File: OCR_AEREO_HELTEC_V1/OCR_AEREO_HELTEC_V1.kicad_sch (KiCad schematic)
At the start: 28 parts, among them J1 INCLINOMETRO, J10 Conn_01x02_Pin, J11 Conn_01x02_Pin, J13 Conn_01x04_Socket, J14 MODULO SD, J15 Conn_01x03_Pin, J16 Conn_01x04_Socket, J17 Screw_Terminal_01x03, J18 Screw_Terminal_01x03, J19 Screw_Terminal_01x02, J3 Conn_01x18_Pin, J4 Conn_01x02_Pin, J5 Conn_01x02_Pin, J6 Screw_Terminal_01x04, J7 Screw_Terminal_01x02, J8 Conn_01x02_Pin, J9 Conn_01x02_Pin, U2 MAX3232

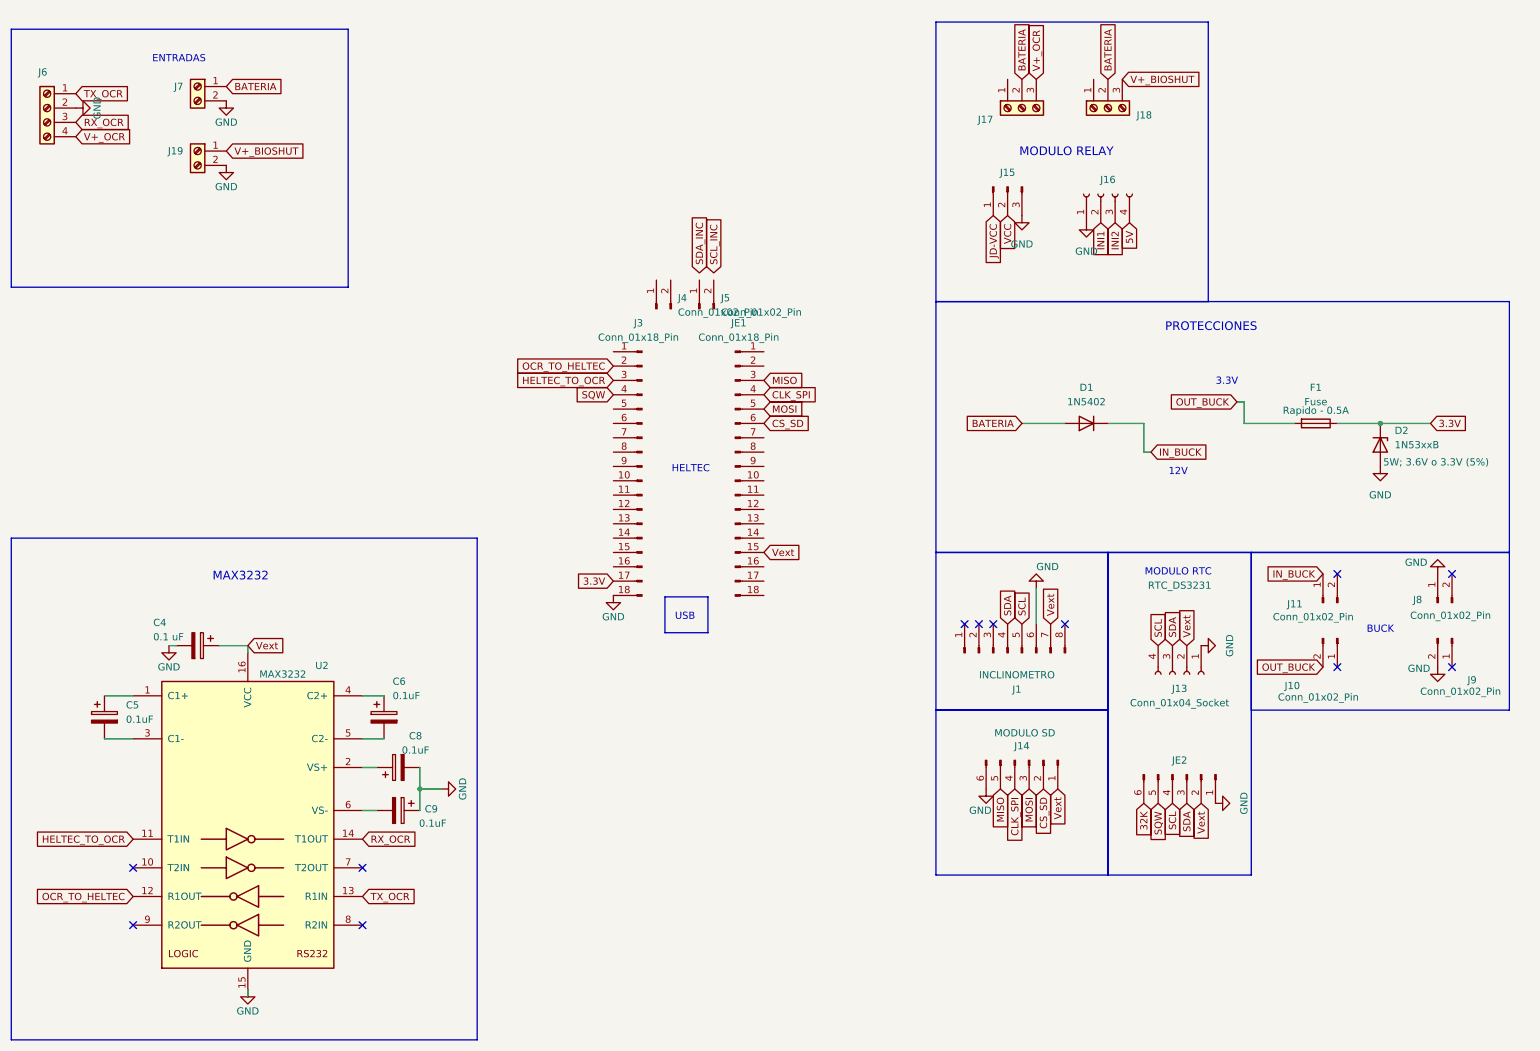
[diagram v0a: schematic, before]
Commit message: Actualizacion de placa
Incluye diseño de PCB con cotas y disposición de ocmponentes actualizadas.

Incluye ambos inclinometros
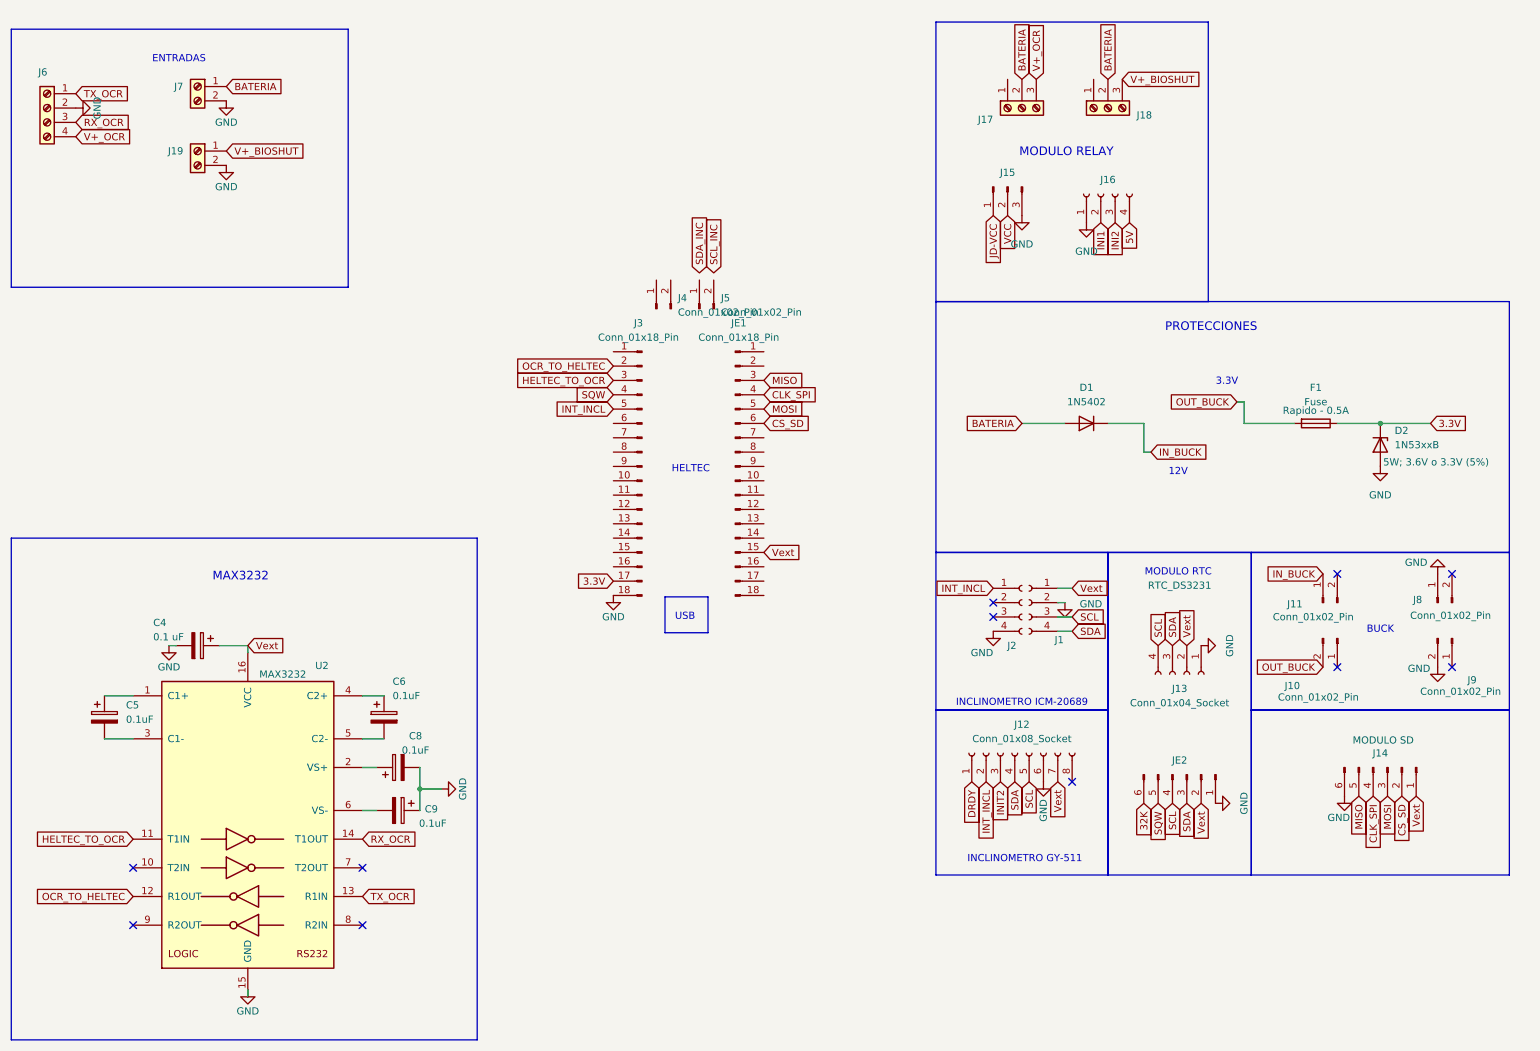
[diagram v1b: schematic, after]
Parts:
- removed J1: INCLINOMETRO, Connector_PinHeader_2.54mm:PinHeader_1x08_P2.54mm_Horizontal, symbol Connector:Conn_01x08_Pin
- added J1, J2: Conn_01x04_Socket, Connector_PinHeader_2.54mm:PinHeader_1x04_P2.54mm_Vertical, symbol Connector:Conn_01x04_Socket
- added J12: Conn_01x08_Socket, Connector_PinHeader_2.54mm:PinHeader_1x08_P2.54mm_Vertical, symbol Connector:Conn_01x08_Socket
- C4: footprint Capacitor_THT:CP_Radial_D4.0mm_P2.00mm -> Capacitor_THT:C_Disc_D5.0mm_W2.5mm_P2.50mm
- J14: footprint Connector_PinHeader_2.54mm:PinHeader_1x06_P2.54mm_Horizontal -> Connector_PinSocket_2.54mm:PinSocket_1x06_P2.54mm_Horizontal
- J19: value Screw_Terminal_01x02 -> BIOSHUT
- J6: value Screw_Terminal_01x04 -> OCR
- J7: value Screw_Terminal_01x02 -> BATERÍA
- JE2: footprint Connector_PinHeader_2.54mm:PinHeader_1x06_P2.54mm_Horizontal -> Connector_PinHeader_2.54mm:PinHeader_1x06_P2.54mm_Vertical
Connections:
- net GND: now also J1.2 (Pin_2), J12.6 (Pin_6), J2.4 (Pin_4)
- net SCL: now also J1.3 (Pin_3), J12.5 (Pin_5)
- net SDA: now also J1.4 (Pin_4), J12.4 (Pin_4)
- net Vext: now also J1.1 (Pin_1), J12.7 (Pin_7)
- net INT_INCL: now reaches J3.5 (Pin_5)
- net INT_INCL: now also J12.2 (Pin_2), J2.1 (Pin_1)
- new net DRDY: J12.1 (Pin_1)
- new net INIT2: J12.3 (Pin_3)
- no-connect marks 12 -> 11
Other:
- note added: "INCLINOMETRO GY-511"
- note added: "INCLINOMETRO ICM-20689"
- moved on the sheet: J14

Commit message: actualizacion V2
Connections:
- net SCL: now also J5.2 (Pin_2)
- net SDA: now also J5.1 (Pin_1)
- net INT_INCL_2: now reaches J3.6 (Pin_6)
- net INT_INCL_2: now also J12.2 (Pin_2)
- net INT_INCL renamed INT_INCL_1
- net INT_INCL_1: no longer J12.2 (Pin_2)
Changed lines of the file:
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@@
+		)
+	)
+	(global_label "INT_INCL_2"
+		(shape input)
+		(at 121.92 85.09 180)
+		(fields_autoplaced yes)
+		(effects
+			(font
+				(size 1.27 1.27)
+			)
+			(justify right)
+		)
+		(property "Intersheetrefs" "${INTERSHEET_REFS}"
+			(at 108.6538 85.09 0)
+			(hide yes)
+			(show_name no)
+			(do_not_autoplace no)
+			(effects
+				(font
+					(size 1.27 1.27)
+				)
+				(justify right)
+			)
 		)
 	)
@@
 		)
 	)
-	(global_label "SCL_INC"
-		(shape input)
-		(at 139.7 58.42 90)
-		(fields_autoplaced yes)
-		(effects
-			(font
-				(size 1.27 1.27)
-			)
-			(justify left)
-		)
-		(property "Intersheetrefs" "${INTERSHEET_REFS}"
-			(at 139.7 47.7543 90)
-			(hide yes)
-			(show_name no)
-			(do_not_autoplace no)
-			(effects
-				(font
-					(size 1.27 1.27)
-				)
-				(justify left)
-			)
-		)
-	)
 	(global_label "SCL"
 		(shape input)
+		(at 139.7 59.69 90)
+		(fields_autoplaced yes)
+		(effects
+			(font
+				(size 1.27 1.27)
+			)
+			(justify left)
+		)
+		(property "Intersheetrefs" "${INTERSHEET_REFS}"
+			(at 139.7 53.1972 90)
+			(hide yes)
+			(show_name no)
+			(do_not_autoplace no)
+			(effects
+				(font
+					(size 1.27 1.27)
+				)
+				(justify left)
+			)
+		)
+	)
+	(global_label "SCL"
+		(shape input)
 		(at 218.44 124.46 90)
 		(fields_autoplaced yes)
@@
 		)
 	)
-	(global_label "INT_INCL"
+	(global_label "INT_INCL_2"
 		(shape input)
 		(at 187.96 148.59 270)
@@
 		)
 		(property "Intersheetrefs" "${INTERSHEET_REFS}"
-			(at 187.96 159.6791 90)
+			(at 187.96 161.8562 90)
 			(hide yes)
 			(show_name no)
@@
 		)
 	)
-	(global_label "SDA_INC"
-		(shape input)
-		(at 137.16 58.42 90)
-		(fields_autoplaced yes)
-		(effects
-			(font
-				(size 1.27 1.27)
-			)
-			(justify left)
-		)
-		(property "Intersheetrefs" "${INTERSHEET_REFS}"
-			(at 137.16 47.6938 90)
+	(global_label "SDA"
+		(shape input)
+		(at 137.16 59.69 90)
+		(fields_autoplaced yes)
+		(effects
+			(font
+				(size 1.27 1.27)
+			)
+			(justify left)
+		)
+		(property "Intersheetrefs" "${INTERSHEET_REFS}"
+			(at 137.16 53.1367 90)
 			(hide yes)
 			(show_name no)
@@
 		)
 	)
-	(global_label "INT_INCL"
+	(global_label "INT_INCL_1"
 		(shape input)
 		(at 121.92 82.55 180)
@@
 		)
 		(property "Intersheetrefs" "${INTERSHEET_REFS}"
-			(at 110.8309 82.55 0)
-			(hide yes)
-			(show_name no)
-			(do_not_autoplace no)
-			(effects
-				(font
-					(size 1.27 1.27)
-				)
-				(justify right)
-			)
-		)
-	)
-	(global_label "INT_INCL"
+			(at 108.6538 82.55 0)
+			(hide yes)
+			(show_name no)
+			(do_not_autoplace no)
+			(effects
+				(font
+					(size 1.27 1.27)
+				)
+				(justify right)
+			)
+		)
+	)
+	(global_label "INT_INCL_1"
 		(shape input)
 		(at 189.23 114.3 180)
@@
 		)
 		(property "Intersheetrefs" "${INTERSHEET_REFS}"
-			(at 178.1409 114.3 0)
-			(hide yes)
-			(show_name no)
+			(at 175.9638 114.3 0)
+			(hide yes)
+			(show_name no)

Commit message: v3 actualizada
incluye pcb routeado
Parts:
- added C7: 470uF, Capacitor_THT:CP_Radial_D4.0mm_P2.00mm, symbol Device:C_Polarized
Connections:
- net 5V: now also D2.1 (K), F1.1, J14.2 (Pin_2), JE1.17 (Pin_17), C7.1
- net CLK_SPI: now also J14.5 (Pin_5), JE1.3 (Pin_3); no longer J14.4 (Pin_4), JE1.4 (Pin_4)
- net CS_SD: now also J14.6 (Pin_6); no longer J14.2 (Pin_2)
- net GND: now also J14.1 (Pin_1), C7.2; no longer J14.6 (Pin_6)
- net MISO: now also J14.3 (Pin_3), JE1.5 (Pin_5); no longer J14.5 (Pin_5), JE1.3 (Pin_3)
- net MOSI: now also J14.4 (Pin_4), JE1.4 (Pin_4); no longer J14.3 (Pin_3), JE1.5 (Pin_5)
- net Vext: no longer J14.1 (Pin_1)
- removed net 3.3V: D2.1 (K), F1.1, J3.17 (Pin_17)
